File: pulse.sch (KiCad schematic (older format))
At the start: 85 parts, among them J1 D-, J10 OUT_12V, J11 OUT_24V, J12 OUT_5V, J13 USB4085-GF-A_REVA, J2 D+, J3 OUT_VUSB, J4 Conn_01x05_Male, J5 EN_3v3, J6 EN_5V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

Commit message: Fix inductor footprint and routing
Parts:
- L1, L2, L3, L4: footprint isomorph:L_Bourns_SRR1210A_3D -> isomorph:L_Bourns_SRR1208
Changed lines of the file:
@@
 F 0 "L4" V 8450 1850 50  0000 L CNN
 F 1 "SRR1280-221K" V 8300 1350 50  0000 L CNN
-F 2 "isomorph:L_Bourns_SRR1210A_3D" H 8200 1750 50  0001 C CNN
+F 2 "isomorph:L_Bourns_SRR1208" H 8200 1750 50  0001 C CNN
 F 3 "~" H 8200 1750 50  0001 C CNN
 	1    8200 1750
@@
 F 0 "L3" V 8400 5400 50  0000 L CNN
 F 1 "SRR1280-221K" V 8250 4900 50  0000 L CNN
-F 2 "isomorph:L_Bourns_SRR1210A_3D" H 8150 5500 50  0001 C CNN
+F 2 "isomorph:L_Bourns_SRR1208" H 8150 5500 50  0001 C CNN
 F 3 "~" H 8150 5500 50  0001 C CNN
 	1    8150 5500
@@
 F 0 "L2" V 8400 4050 50  0000 L CNN
 F 1 "SRR1280-221K" V 8250 3550 50  0000 L CNN
-F 2 "isomorph:L_Bourns_SRR1210A_3D" H 8150 4150 50  0001 C CNN
+F 2 "isomorph:L_Bourns_SRR1208" H 8150 4150 50  0001 C CNN
 F 3 "~" H 8150 4150 50  0001 C CNN
 	1    8150 4150
@@
 F 0 "L1" V 8400 2650 50  0000 L CNN
 F 1 "SRR1280-221K" V 8250 2150 50  0000 L CNN
-F 2 "isomorph:L_Bourns_SRR1210A_3D" H 8150 2750 50  0001 C CNN
+F 2 "isomorph:L_Bourns_SRR1208" H 8150 2750 50  0001 C CNN
 F 3 "~" H 8150 2750 50  0001 C CNN
 	1    8150 2750

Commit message: Change timing resistor value for 3v3 buck
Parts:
- C6: value 1500pF -> 470pF
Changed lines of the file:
@@
 P 6750 1900
 F 0 "C6" H 6800 2000 50  0000 L CNN
-F 1 "1500pF" H 6750 1800 50  0000 L CNN
+F 1 "470pF" H 6750 1800 50  0000 L CNN
 F 2 "Capacitor_SMD:C_0805_2012Metric" H 6788 1750 50  0001 C CNN
 F 3 "~" H 6750 1900 50  0001 C CNN

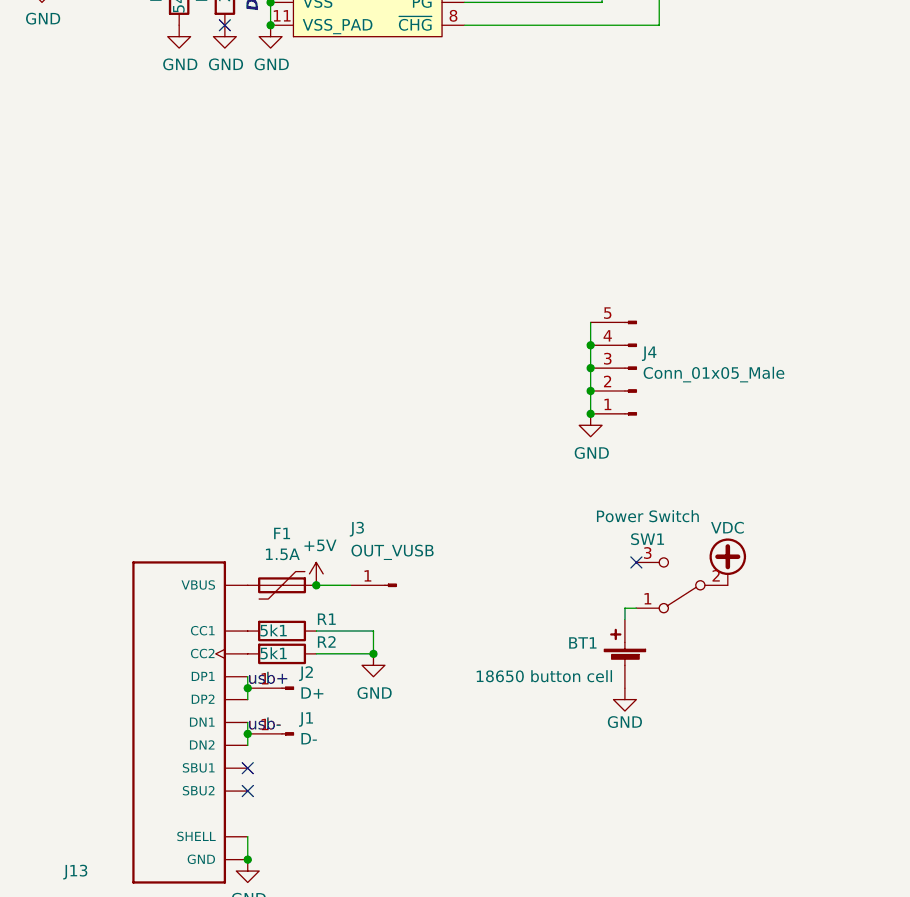
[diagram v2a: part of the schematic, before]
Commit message: Add batteryless operation jumper pads
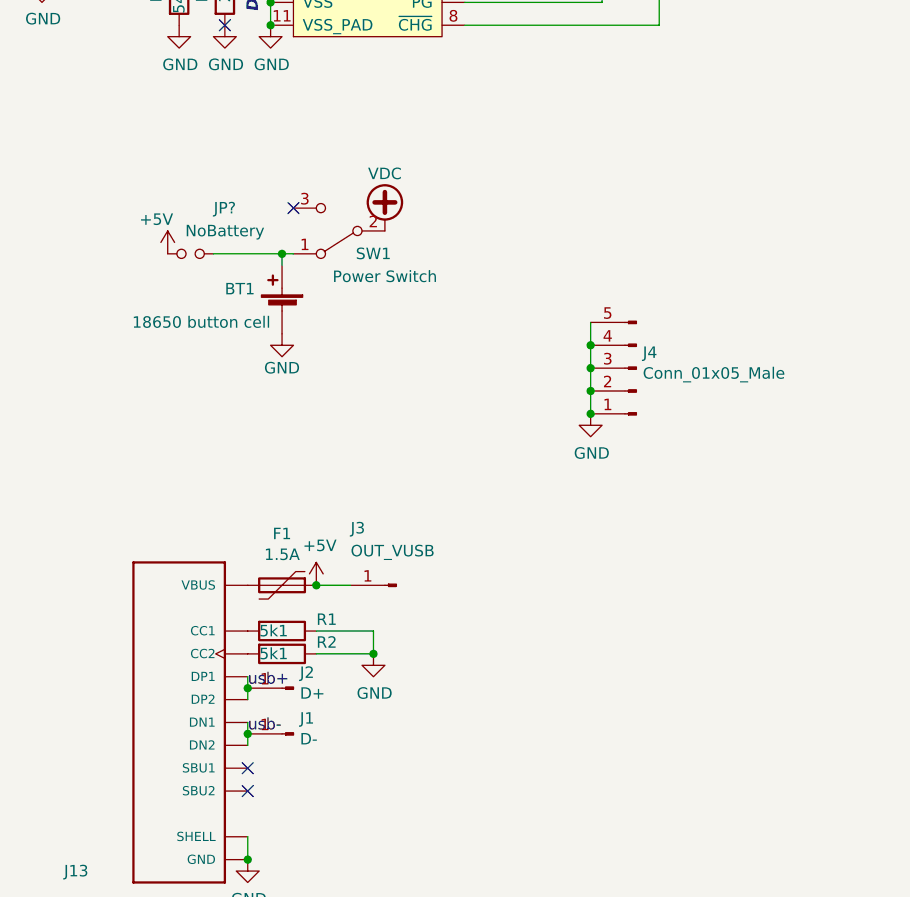
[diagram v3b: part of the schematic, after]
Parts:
- added JP?: NoBattery, symbol Device:Jumper_NO_Small
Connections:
- net +5V: now also JP?.1
- net at BT1.1 (+), SW1.1 (A): now also JP?.2
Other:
- moved on the sheet: BT1, SW1
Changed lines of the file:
@@
 L Switch:SW_SPDT SW1
 U 1 1 5E8AB9F0
-P 4300 4500
-F 0 "SW1" H 4450 4300 50  0000 C CNN
-F 1 "Power Switch" H 4450 4200 50  0000 C CNN
-F 2 "Connector_PinHeader_2.54mm:PinHeader_1x03_P2.54mm_Vertical" H 4300 4500 50  0001 C CNN
-F 3 "~" H 4300 4500 50  0001 C CNN
-	1    4300 4500
+P 2800 2950
+F 0 "SW1" H 2650 3050 50  0000 C CNN
+F 1 "Power Switch" H 2600 3150 50  0000 C CNN
+F 2 "Connector_PinHeader_2.54mm:PinHeader_1x03_P2.54mm_Vertical" H 2800 2950 50  0001 C CNN
+F 3 "~" H 2800 2950 50  0001 C CNN
+	1    2800 2950
 	-1   0    0    1
 $EndComp
@@
 L power:VDC #PWR0147
 U 1 1 5E8AC7C2
-P 4500 4500
-F 0 "#PWR0147" H 4500 4400 50  0001 C CNN
-F 1 "VDC" H 4500 4750 50  0000 C CNN
-F 2 "" H 4500 4500 50  0001 C CNN
-F 3 "" H 4500 4500 50  0001 C CNN
-	1    4500 4500
+P 3000 2950
+F 0 "#PWR0147" H 3000 2850 50  0001 C CNN
+F 1 "VDC" H 3000 3200 50  0000 C CNN
+F 2 "" H 3000 2950 50  0001 C CNN
+F 3 "" H 3000 2950 50  0001 C CNN
+	1    3000 2950
 	1    0    0    -1
 $EndComp
-NoConn ~ 4100 4400
 $Comp
 L Device:Battery_Cell BT1
 U 1 1 5E8B50EA
-P 4050 4850
-F 0 "BT1" H 4168 4946 50  0000 L CNN
-F 1 "18650 button cell" H 4100 4800 50  0000 L CNN
-F 2 "Battery:BatteryHolder_MPD_BH-18650-PC2" V 4050 4910 50  0001 C CNN
-F 3 "~" V 4050 4910 50  0001 C CNN
-	1    4050 4850
+P 2550 3300
+F 0 "BT1" H 2668 3396 50  0000 L CNN
+F 1 "18650 button cell" H 2600 3250 50  0000 L CNN
+F 2 "Battery:BatteryHolder_MPD_BH-18650-PC2" V 2550 3360 50  0001 C CNN
+F 3 "~" V 2550 3360 50  0001 C CNN
+	1    2550 3300
 	-1   0    0    -1
 $EndComp
@@
 L power:GND #PWR0148
 U 1 1 5E8B621D
-P 4050 4950
-F 0 "#PWR0148" H 4050 4700 50  0001 C CNN
-F 1 "GND" H 4050 4800 50  0000 C CNN
-F 2 "" H 4050 4950 50  0001 C CNN
-F 3 "" H 4050 4950 50  0001 C CNN
-	1    4050 4950
+P 2550 3400
+F 0 "#PWR0148" H 2550 3150 50  0001 C CNN
+F 1 "GND" H 2550 3250 50  0000 C CNN
+F 2 "" H 2550 3400 50  0001 C CNN
+F 3 "" H 2550 3400 50  0001 C CNN
+	1    2550 3400
 	1    0    0    -1
 $EndComp
 Wire Wire Line
-	4050 4650 4050 4600
+	2550 3100 2550 3050
 Wire Wire Line
-	4050 4600 4100 4600
+	2550 3050 2600 3050
 $Comp
 L Mechanical:MountingHole H1
@@
 Connection ~ 2700 4500
 Connection ~ 2400 5700
+$Comp
+L power:+5V #PWR?
+U 1 1 5E7527DD
+P 2050 3050
+F 0 "#PWR?" H 2050 2900 50  0001 C CNN
+F 1 "+5V" H 2000 3200 50  0000 C CNN
+F 2 "" H 2050 3050 50  0001 C CNN
+F 3 "" H 2050 3050 50  0001 C CNN
+	1    2050 3050
+	1    0    0    -1
+$EndComp
+NoConn ~ 2600 2850
+$Comp
+L Device:Jumper_NO_Small JP?
+U 1 1 5E7790F0
+P 2150 3050
+F 0 "JP?" H 2300 3250 50  0000 C CNN
+F 1 "NoBattery" H 2300 3150 50  0000 C CNN
+F 2 "" H 2150 3050 50  0001 C CNN
+F 3 "~" H 2150 3050 50  0001 C CNN
+	1    2150 3050
+	1    0    0    -1
+$EndComp
+Wire Wire Line
+	2550 3050 2250 3050
+Connection ~ 2550 3050
 $EndSCHEMATC

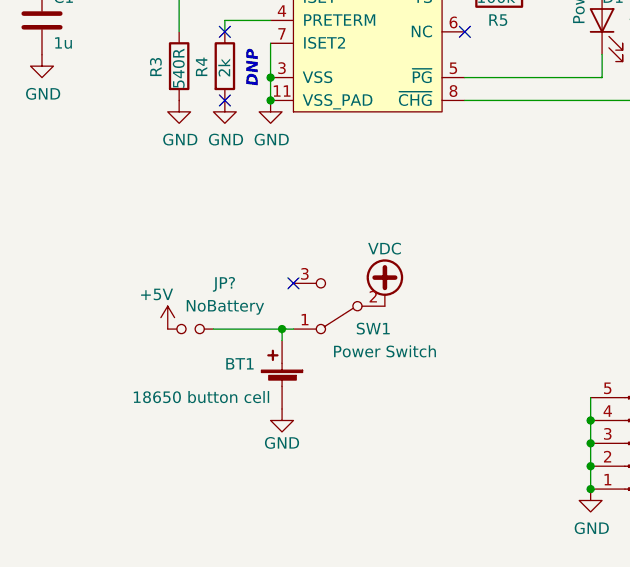
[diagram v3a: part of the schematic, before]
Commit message: Change 0.22R shunt resistors to 1206
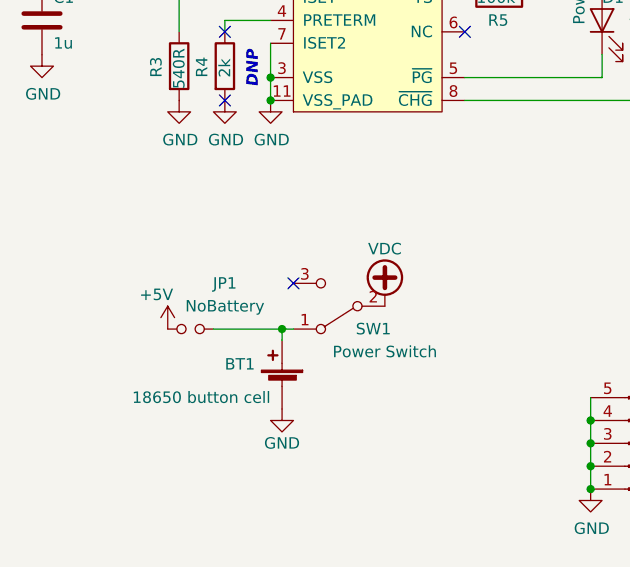
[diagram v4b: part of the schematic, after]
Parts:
- JP1: renamed from JP?; footprint (none) -> Jumper:SolderJumper-2_P1.3mm_Open_Pad1.0x1.5mm
- R16, R17, R18, R19: footprint Resistor_SMD:R_0805_2012Metric -> Resistor_SMD:R_1206_3216Metric
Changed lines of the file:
@@
 F 0 "R18" V 7700 3750 50  0000 L CNN
 F 1 "0R22" V 7600 3700 50  0000 L CNN
-F 2 "Resistor_SMD:R_0805_2012Metric" V 7530 3800 50  0001 C CNN
+F 2 "Resistor_SMD:R_1206_3216Metric" V 7530 3800 50  0001 C CNN
 F 3 "~" H 7600 3800 50  0001 C CNN
 	1    7600 3800
@@
 F 0 "R16" V 7250 1050 50  0000 L CNN
 F 1 "0R22" V 7150 1000 50  0000 L CNN
-F 2 "Resistor_SMD:R_0805_2012Metric" V 7080 1100 50  0001 C CNN
+F 2 "Resistor_SMD:R_1206_3216Metric" V 7080 1100 50  0001 C CNN
 F 3 "~" H 7150 1100 50  0001 C CNN
 	1    7150 1100
@@
 F 0 "R19" V 7700 5100 50  0000 L CNN
 F 1 "0R22" V 7600 5050 50  0000 L CNN
-F 2 "Resistor_SMD:R_0805_2012Metric" V 7530 5150 50  0001 C CNN
+F 2 "Resistor_SMD:R_1206_3216Metric" V 7530 5150 50  0001 C CNN
 F 3 "~" H 7600 5150 50  0001 C CNN
 	1    7600 5150
@@
 F 0 "R17" V 7700 2350 50  0000 L CNN
 F 1 "0R22" V 7600 2300 50  0000 L CNN
-F 2 "Resistor_SMD:R_0805_2012Metric" V 7530 2400 50  0001 C CNN
+F 2 "Resistor_SMD:R_1206_3216Metric" V 7530 2400 50  0001 C CNN
 F 3 "~" H 7600 2400 50  0001 C CNN
 	1    7600 2400
@@
 Connection ~ 2400 5700
 $Comp
-L power:+5V #PWR?
+L power:+5V #PWR0149
 U 1 1 5E7527DD
 P 2050 3050
-F 0 "#PWR?" H 2050 2900 50  0001 C CNN
+F 0 "#PWR0149" H 2050 2900 50  0001 C CNN
 F 1 "+5V" H 2000 3200 50  0000 C CNN
 F 2 "" H 2050 3050 50  0001 C CNN
@@
 NoConn ~ 2600 2850
 $Comp
-L Device:Jumper_NO_Small JP?
+L Device:Jumper_NO_Small JP1
 U 1 1 5E7790F0
 P 2150 3050
-F 0 "JP?" H 2300 3250 50  0000 C CNN
+F 0 "JP1" H 2300 3250 50  0000 C CNN
 F 1 "NoBattery" H 2300 3150 50  0000 C CNN
-F 2 "" H 2150 3050 50  0001 C CNN
+F 2 "Jumper:SolderJumper-2_P1.3mm_Open_Pad1.0x1.5mm" H 2150 3050 50  0001 C CNN
 F 3 "~" H 2150 3050 50  0001 C CNN
 	1    2150 3050

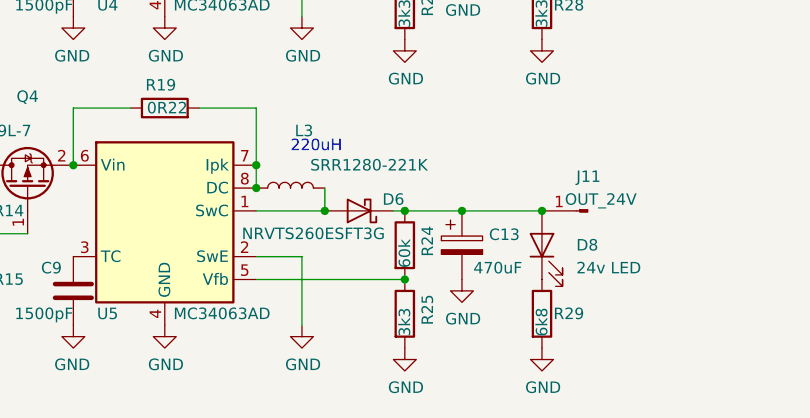
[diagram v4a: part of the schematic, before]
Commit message: Change 24vfb resistors to more common value
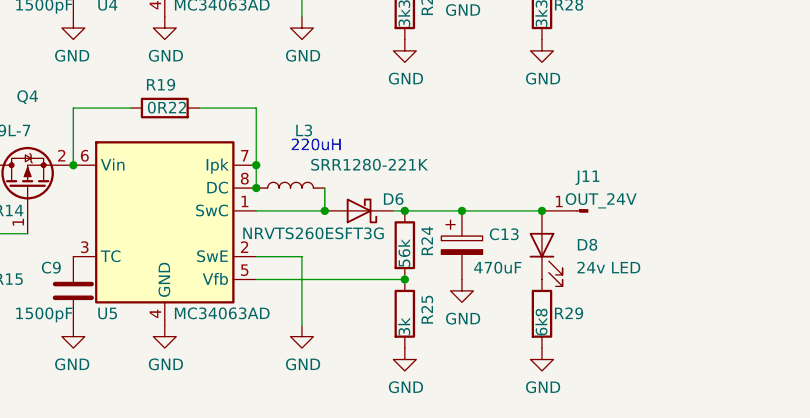
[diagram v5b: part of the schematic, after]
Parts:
- R24: value 60k -> 56k
- R25: value 3k3 -> 3k
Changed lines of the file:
@@
 P 8650 5750
 F 0 "R24" V 8750 5700 50  0000 L CNN
-F 1 "60k" V 8650 5650 50  0000 L CNN
+F 1 "56k" V 8650 5650 50  0000 L CNN
 F 2 "Resistor_SMD:R_0805_2012Metric" V 8580 5750 50  0001 C CNN
 F 3 "~" H 8650 5750 50  0001 C CNN
@@
 P 8650 6050
 F 0 "R25" V 8750 6000 50  0000 L CNN
-F 1 "3k3" V 8650 5950 50  0000 L CNN
+F 1 "3k" V 8650 5950 50  0000 L CNN
 F 2 "Resistor_SMD:R_0805_2012Metric" V 8580 6050 50  0001 C CNN
 F 3 "~" H 8650 6050 50  0001 C CNN

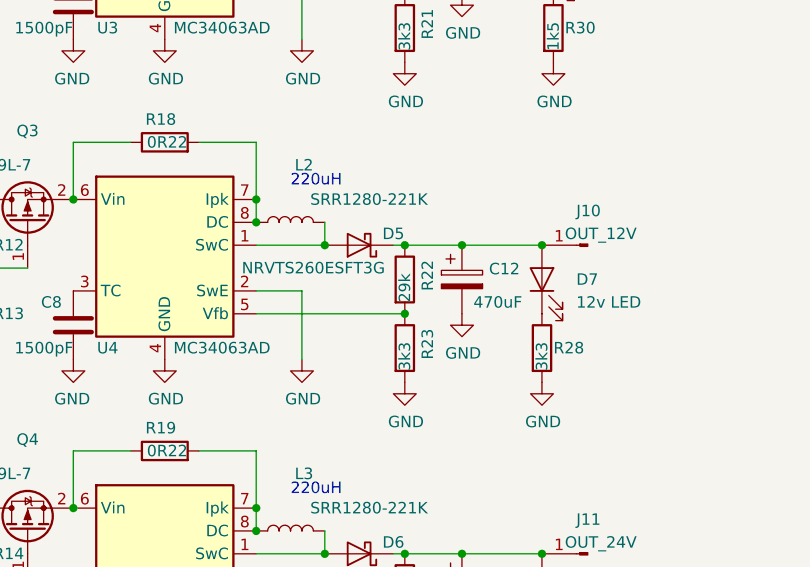
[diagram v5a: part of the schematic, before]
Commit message: Change 12vfb high resistor to more common value
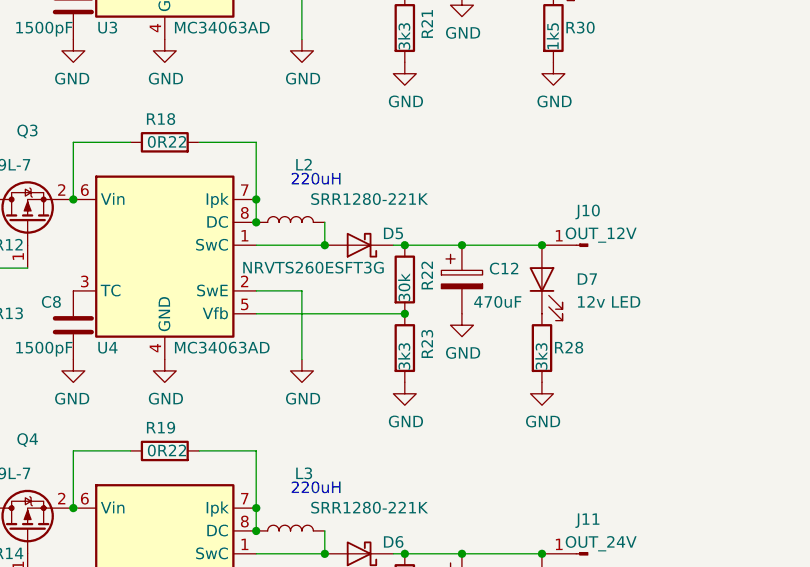
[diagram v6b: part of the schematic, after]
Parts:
- R22: value 29k -> 30k
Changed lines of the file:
@@
 P 8650 4400
 F 0 "R22" V 8750 4350 50  0000 L CNN
-F 1 "29k" V 8650 4300 50  0000 L CNN
+F 1 "30k" V 8650 4300 50  0000 L CNN
 F 2 "Resistor_SMD:R_0805_2012Metric" V 8580 4400 50  0001 C CNN
 F 3 "~" H 8650 4400 50  0001 C CNN
